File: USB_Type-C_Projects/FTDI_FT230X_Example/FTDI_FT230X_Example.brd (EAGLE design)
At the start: 32.5 x 65 mm, 47 parts, among them J1 105450-0101, U1 FT230XQ-R, U135123 P8X32A-Q44, U2 IRLML6401TRPBF, U3 NCP1117LPST33T3G, U4 CAT24C512WI-GT3, X1 ABMM-6.000MHZ-B2-T

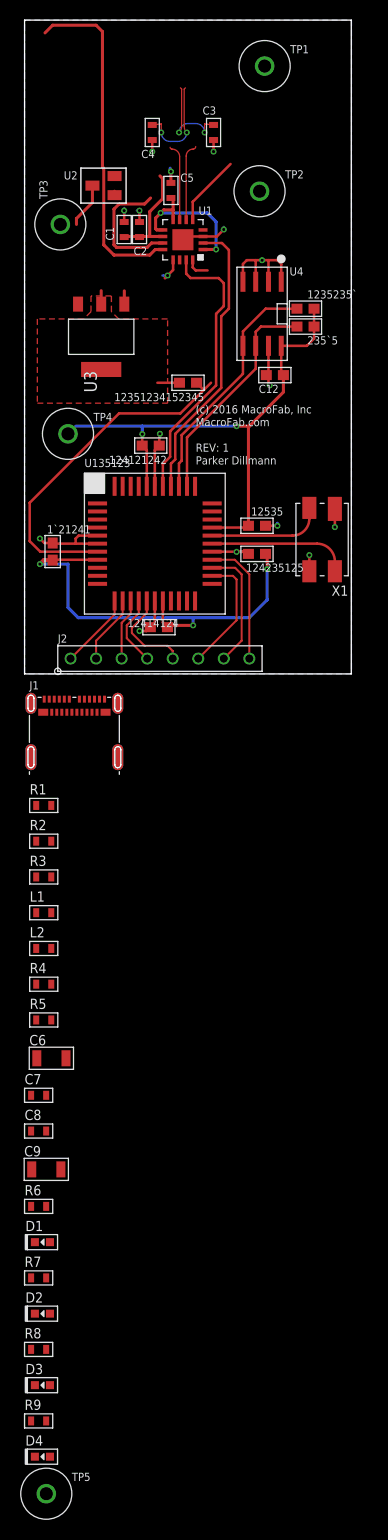
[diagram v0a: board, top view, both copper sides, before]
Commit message: Finished the FTDI_FT230X Example
Prop has been added and a header to monitor the current off the USB buss
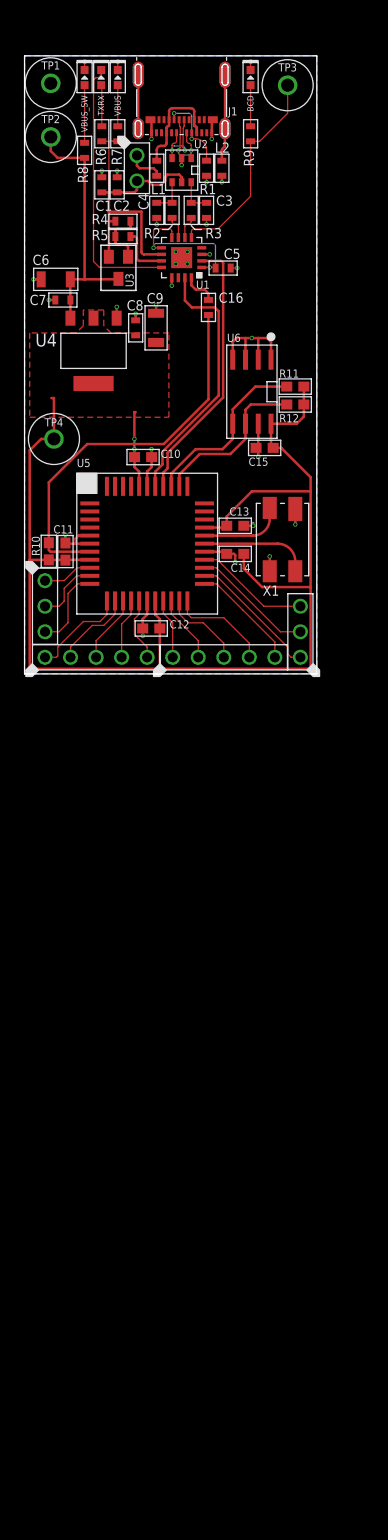
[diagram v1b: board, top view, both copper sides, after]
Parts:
- removed 12351234152345, 1235235`, 235`5: 10K, PP_Passives:0603
- removed 124121242, 12414124, 124235125, 12535, 1`21241: .1uF, PP_Passives:0603
- removed D1, D2, D3, D4: MF-LED-0603-RED, MF_LEDs:LED0603
- removed TP5: (no value), PP_Connectors:KEYSTONE_5115-5119
- removed U135123: P8X32A-Q44, PP_DigitalIC:P8X32A_LQFP-44
- added BCD, TXRX, VBUS, VBUS_SW: MF-LED-0603-RED, MF_LEDs:LED0603
- added C10, C11, C13, C14, C15: .1uF, PP_Passives:0603
- added C16: 0.1uF, MF_Passives:C0603
- added J3: MF-CON-2.54mm-01x02, MF_Connectors:PTH_2.54MM_01X02
- added J4, J6: MF-CON-2.54mm-01x05, MF_Connectors:PTH_2.54MM_01X05
- added J5: MF-CON-2.54mm-01x03, MF_Connectors:PTH_2.54MM_01X03
- added R10, R11, R12: 10K, PP_Passives:0603
- added U5: P8X32A-Q44, PP_DigitalIC:P8X32A_LQFP-44
- added U6: CAT24C512WI-GT3, PP_DigitalIC:SOIC-8_W
- FRAME1: value (none) -> MF_FRAMEDEFAULT
- J2: value (none) -> MF-CON-2.54mm-01x03; device PP_Connectors:2.54MM_01X08_PIN_HEADER -> MF_Connectors:PTH_2.54MM_01X03
- R6: value 150 -> 330
- TP1, TP2, TP3, TP4: value (none) -> 5115
- U2: value IRLML6401TRPBF -> IP4234CZ6,125; device PP_DiscreteSemi:SOT-23-3 -> PP_Passives:IP4234CZ6_SOT-457-6
- U3: value NCP1117LPST33T3G -> IRLML6401TRPBF; device MF_IC_Power:SOT-223-3 -> PP_DiscreteSemi:SOT-23-3
- U4: value CAT24C512WI-GT3 -> NCP1117LPST33T3G; device PP_DigitalIC:SOIC-8_W -> MF_IC_Power:SOT-223-3
- moved R9 129.7 mm to (22.5, 53.7), turned to 90 degrees
- moved R8 119.3 mm to (5.97, 52.1), turned to 90 degrees
- moved R7 114.1 mm to (9.27, 53.7), turned to 90 degrees
- moved R6 106.9 mm to (7.68, 53.7), turned to 90 degrees
- moved C9 84.4 mm to (13.1, 34.4), turned to 90 degrees
- moved C8 80.5 mm to (11.0, 34.4), turned to 90 degrees
- moved L2 79.6 mm to (19.6, 50.3), turned to 270 degrees
- moved C7 79.1 mm to (3.81, 37.2), turned to 180 degrees
- moved R5 78.3 mm to (9.78, 43.5)
- moved C6 77.5 mm to (3.10, 39.2), turned to 180 degrees
- moved R4 76.3 mm to (9.78, 45.0)
- moved L1 74.9 mm to (13.1, 50.3), turned to 270 degrees
- moved R3 67.9 mm to (16.6, 46.1), turned to 270 degrees
- moved R1 65.4 mm to (18.1, 50.3), turned to 270 degrees
- moved R2 64.0 mm to (14.7, 46.1), turned to 270 degrees
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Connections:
- net CC1/2 renamed CC1/1
- removed net N$1: D4.ANODE, R9.P$2
- removed net N$2: D1.ANODE, R6.P$2
- removed net N$41: R4.P$2, R5.P$1, U2.1
- removed net N$5: D2.ANODE, R7.P$2
- removed net N$6: D3.ANODE, R8.P$2
- new net N$10: R6.P$2, TXRX.ANODE
- new net N$11: R7.P$2, VBUS.ANODE
- new net N$12: R8.P$2, VBUS_SW.ANODE
- new net N$13: BCD.ANODE, R9.P$2
- new net N$14: C3.P$1, R3.P$1, U2.6
- new net N$15: C4.P$1, R2.P$1, U2.4
- new net N$8: R4.P$2, R5.P$1, U3.1
- new net SYSTEM_VBUS: C1.P$1, C2.P$1, J3.P$2, R4.P$1, R6.P$1, R7.P$1, U1.10, U2.5, U3.2
- net 3.3V: now also C10.2, C11.2, C13.2, C14.2, C15.2, R10.1, R11.2, R12.2, TP4.P$1, U4.P$1, U4.P$3, U5.18, U5.30, U5.40, U5.8, U6.8; no longer 12351234152345.2, 1235235`.2, 124121242.2, 12414124.2, 124235125.2, 12535.2, 1`21241.2, 235`5.2, R6.P$1, TP5.P$1, U135123.18, U135123.30, U135123.40, U135123.8, U3.P$1, U3.P$3, U4.8
- net BCD_CHARGER: now also TP3.P$1; no longer TP4.P$1
- net D+: now also U2.1; no longer C3.P$1, R3.P$1
- net D-: now also U2.3; no longer C4.P$1, R2.P$1
- net GND: now also BCD.CATHODE, C10.1, C11.1, C13.1, C14.1, C15.1, TP1.P$1, U2.2, U4.P$2, U5.17, U5.27, U5.39, U5.5, U5.6, U6.1, U6.2, U6.3, U6.4, U6.7, VBUS.CATHODE, VBUS_SW.CATHODE; no longer 124121242.1, 12414124.1, 124235125.1, 12535.1, 1`21241.1, D2.CATHODE, D3.CATHODE, D4.CATHODE, TP2.P$1, U135123.17, U135123.27, U135123.39, U135123.5, U135123.6, U3.P$2, U4.1, U4.2, U4.3, U4.4, U4.7
- net P0: now also U5.41; no longer U135123.41
- net P1: now also U5.42; no longer U135123.42
- net P10: now also J2.P$3, U5.11; no longer U135123.11
- net P11: now also J4.P$1, U5.12; no longer J2.1, U135123.12
- net P12: now also J4.P$2, U5.13; no longer J2.2, U135123.13
- net P13: now also J4.P$3, U5.14; no longer J2.3, U135123.14
- net P14: now also J4.P$4, U5.15; no longer J2.4, U135123.15
- net P15: now also J4.P$5, U5.16; no longer J2.5, U135123.16
- net P16: now also J6.P$1, U5.19; no longer U135123.19
- net P17: now also J6.P$2, U5.20; no longer U135123.20
- net P18: now also J6.P$3, U5.21; no longer U135123.21
- net P19: now also J6.P$4, U5.22; no longer U135123.22
- net P2: now also U5.43; no longer U135123.43
- net P20: now also J6.P$5, U5.23; no longer U135123.23
- net P21: now also J5.P$1, U5.24; no longer J2.6, U135123.24
- net P22: now also J5.P$2, U5.25; no longer J2.7, U135123.25
- net P23: now also J5.P$3, U5.26; no longer J2.8, U135123.26
- net P24: now also U5.31; no longer U135123.31
- net P25: now also U5.32; no longer U135123.32
- net P26: now also U5.33; no longer U135123.33
- net P27: now also U5.34; no longer U135123.34
- net P3: now also U5.44; no longer U135123.44
- net P4: now also U5.1; no longer U135123.1
- net P5: now also U5.2; no longer U135123.2
- net P6: now also U5.3; no longer U135123.3
- net P7: now also U5.4; no longer U135123.4
- net P8: now also J2.P$1, U5.9; no longer U135123.9
- net P9: now also J2.P$2, U5.10; no longer U135123.10
- net RES: now also C16.P$2, R10.2, U5.7; no longer 12351234152345.1, U135123.7
- net RTS: now also C16.P$1
- net RX: now also U5.37; no longer U135123.37
- net SCL: now also R12.1, U5.35, U6.6; no longer 235`5.1, U135123.35, U4.6
- net SDA: now also R11.1, U5.36, U6.5; no longer 1235235`.1, U135123.36, U4.5
- net TX: now also U5.38; no longer U135123.38
- net TX_RX_LED: now also TXRX.CATHODE; no longer D1.CATHODE
- net USB_VBUS: now also J3.P$1; no longer C1.P$1, C2.P$1, R4.P$1, R7.P$1, U1.10, U2.2
- net USB_VBUS_PORT: no longer TP1.P$1
- net USB_VBUS_SWITCHED: now also TP2.P$1, U3.3, U4.P$4; no longer TP3.P$1, U2.3, U3.P$4
- net X0: now also U5.29; no longer U135123.29
- net X1: now also U5.28; no longer U135123.28
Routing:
- net SYSTEM_VBUS: track 0.00 -> 34.3 mm
- net 3.3V: track 101.6 -> 132.4 mm, vias 5 -> 2
- net USB_VBUS_SWITCHED: track 4.73 -> 28.9 mm
- net N$9: track 0.00 -> 14.1 mm
- net BCD_CHARGER: track 7.09 -> 21.0 mm
- net P20: track 0.00 -> 10.9 mm
- net USB_VBUS_PORT: track 0.00 -> 10.6 mm
- net P19: track 0.00 -> 10.0 mm
- net CC1/1: track 0.00 -> 8.38 mm, vias 0 -> 2
- net P18: track 0.00 -> 8.33 mm
- net P10: track 0.00 -> 8.14 mm
- net PWREN: track 12.8 -> 5.21 mm
- net TX_RX_LED: track 34.1 -> 26.5 mm
- net USB_VBUS: track 10.7 -> 3.65 mm
- net P17: track 0.00 -> 6.71 mm
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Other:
- board size 32.5 x 65 mm -> 29.1 x 61.5 mm

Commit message: Added MPNs and normalized part values
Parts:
- C10, C11, C12, C13, C14, C15: value .1uF -> 0.1uF

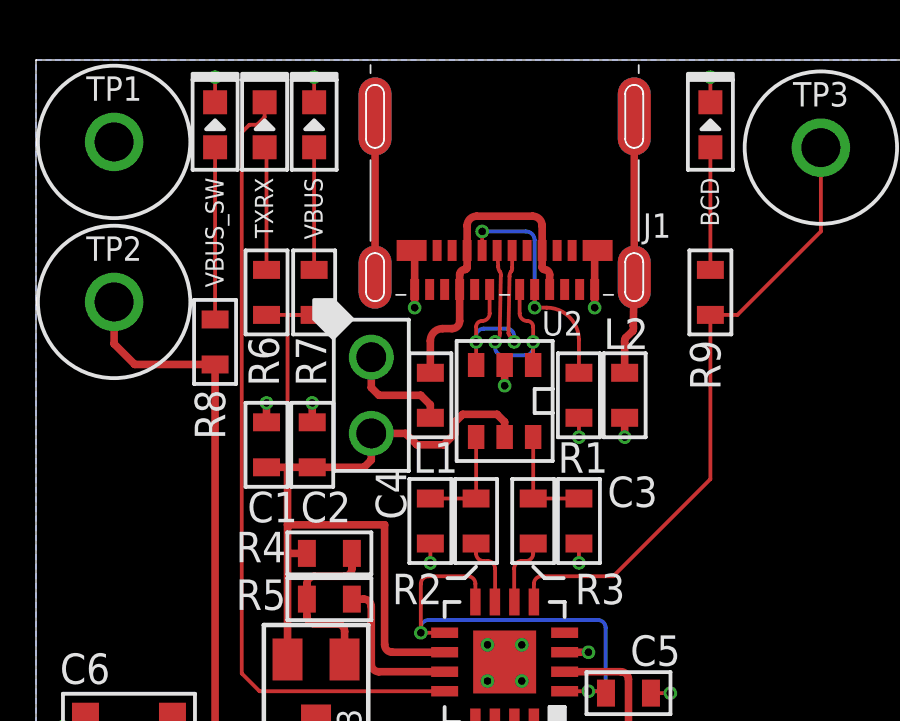
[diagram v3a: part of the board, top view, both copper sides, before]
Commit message: Fixed IP4234CZ6 ESD protection
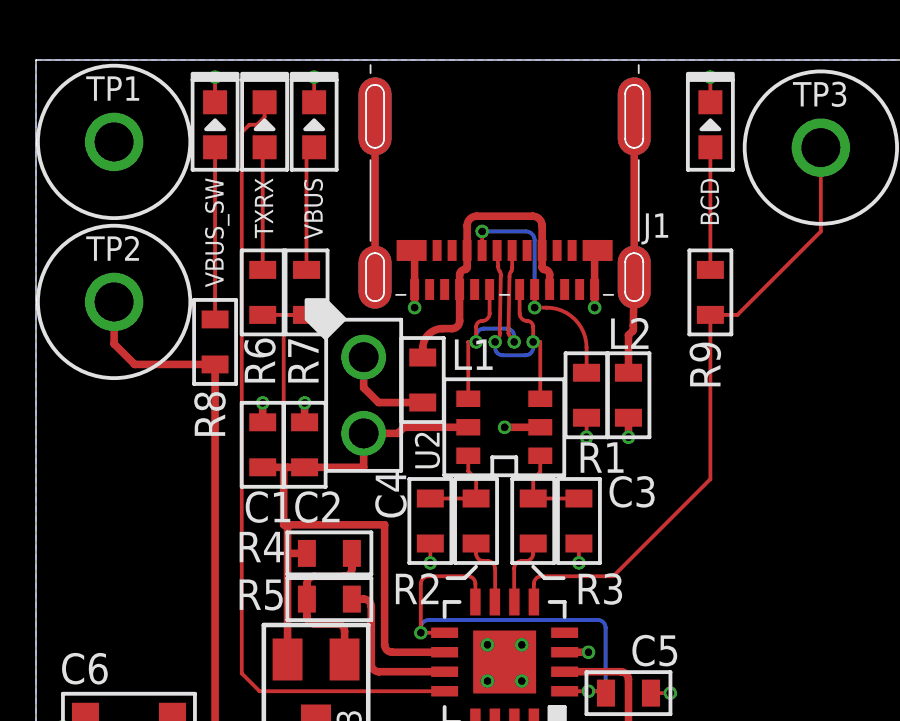
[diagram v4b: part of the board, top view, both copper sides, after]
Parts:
- moved U2 0.88 mm to (15.6, 49.2), turned to 180 degrees
- moved L1 0.57 mm to (12.9, 50.8)
- moved R1 0.25 mm to (18.4, 50.3)
- moved R7 0.25 mm to (9.02, 53.7)
- moved C2 0.25 mm to (8.95, 48.6)
- moved J3 0.25 mm to (10.9, 50.3)
- moved C1 0.13 mm to (7.56, 48.6)
- moved R6 0.13 mm to (7.56, 53.7)
- moved L2 0.13 mm to (19.7, 50.3)
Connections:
- net D+: now also U2.3; no longer U2.1
- net D-: now also U2.4; no longer U2.3
- net N$14: now also U2.1; no longer U2.6
- net N$15: now also U2.6; no longer U2.4
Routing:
- net SYSTEM_VBUS: track 34.3 -> 32.4 mm
- net D-: track 7.68 -> 9.07 mm
- net D+: track 7.68 -> 9.04 mm
- net N$14: track 3.58 -> 3.05 mm
- net N$15: track 3.58 -> 3.06 mm

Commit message: REV 2. Fixed USB ESD protection.
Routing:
- net SYSTEM_VBUS: track 32.4 -> 31.3 mm
- net 3.3V: track 132.4 -> 131.6 mm
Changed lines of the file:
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@@
 <?xml version="1.0" encoding="utf-8"?>
 <!DOCTYPE eagle SYSTEM "eagle.dtd">
-<eagle version="9.3.0">
+<eagle version="9.3.2">
 <drawing>
 <settings>
@@
 <attribute name="MPN" value="" x="0.889" y="11.176" size="1.778" layer="28" rot="MR180" display="off"/>
 <attribute name="POPULATE" value="0" x="0.889" y="11.176" size="1.778" layer="28" rot="MR180" display="off"/>
-<attribute name="REVNUM" value="REV: 1" x="0.889" y="16.256" size="0.8128" layer="22" font="vector" ratio="16" rot="MR180"/>
+<attribute name="REVNUM" value="REV: 2" x="0.889" y="16.256" size="0.8128" layer="22" font="vector" ratio="16" rot="MR180"/>
 <attribute name="URL" value="" x="0.889" y="11.176" size="1.778" layer="28" rot="MR180" display="off"/>
 </element>
@@
 <wire x1="1.651" y1="23.368" x2="0.508" y2="22.225" width="0.254" layer="1"/>
 <wire x1="0.508" y1="22.225" x2="0.508" y2="11.342" width="0.254" layer="1"/>
-<wire x1="0.508" y1="11.342" x2="0.508" y2="0.508" width="0.254" layer="1"/>
-<wire x1="0.508" y1="0.508" x2="13.4484" y2="0.508" width="0.254" layer="1"/>
-<wire x1="13.4484" y1="0.508" x2="28.448" y2="0.508" width="0.254" layer="1"/>
-<wire x1="28.448" y1="0.508" x2="28.448" y2="8.636" width="0.254" layer="1"/>
+<wire x1="0.508" y1="11.342" x2="0.508" y2="1.397" width="0.254" layer="1"/>
+<wire x1="0.508" y1="1.397" x2="1.397" y2="0.508" width="0.254" layer="1"/>
+<wire x1="1.397" y1="0.508" x2="13.4484" y2="0.508" width="0.254" layer="1"/>
+<wire x1="13.4484" y1="0.508" x2="27.94" y2="0.508" width="0.254" layer="1"/>
+<wire x1="27.94" y1="0.508" x2="28.448" y2="1.016" width="0.254" layer="1"/>
+<wire x1="28.448" y1="1.016" x2="28.448" y2="8.636" width="0.254" layer="1"/>
 <wire x1="28.448" y1="8.636" x2="28.448" y2="18.161" width="0.254" layer="1"/>
 <wire x1="28.448" y1="18.161" x2="28.448" y2="19.558" width="0.254" layer="1"/>
@@
 <contactref element="J1" pad="B6"/>
 <contactref element="U2" pad="3"/>
-<wire x1="16.571" y1="52.07" x2="16.8083" y2="52.07" width="0.127" layer="1"/>
-<wire x1="16.8083" y1="52.07" x2="16.8083" y2="50.1752" width="0.127" layer="1"/>
+<wire x1="16.571" y1="52.07" x2="16.8083" y2="51.8327" width="0.127" layer="1"/>
+<wire x1="16.8083" y1="51.8327" x2="16.8083" y2="50.1752" width="0.127" layer="1"/>
 </signal>
 <signal name="3V3OUT">
@@
 <contactref element="J1" pad="B7"/>
 <contactref element="U2" pad="4"/>
-<wire x1="14.671" y1="52.07" x2="14.4083" y2="52.07" width="0.127" layer="1"/>
-<wire x1="14.4083" y1="52.07" x2="14.4083" y2="50.1752" width="0.127" layer="1"/>
+<wire x1="14.671" y1="52.07" x2="14.4083" y2="51.8073" width="0.127" layer="1"/>
+<wire x1="14.4083" y1="51.8073" x2="14.4083" y2="50.1752" width="0.127" layer="1"/>
 </signal>
 <signal name="PWREN">
@@
 <wire x1="19.941" y1="59.589" x2="19.941" y2="54.10665" width="0.254" layer="1"/>
 <wire x1="19.941" y1="54.10665" x2="19.93678125" y2="54.10665" width="0.254" layer="1"/>
-<wire x1="11.301" y1="54.229" x2="19.7485" y2="52.297853125" width="0" layer="19" extent="1-1"/>
+<wire x1="11.301" y1="59.589" x2="19.941" y2="59.589" width="0" layer="19" extent="1-1"/>
 </signal>
 <signal name="BCD_CHARGER">
@@
 <wire x1="8.3845" y1="45.0215" x2="8.3845" y2="45.974" width="0.254" layer="1"/>
 <wire x1="9.029" y1="45.0215" x2="8.3845" y2="45.0215" width="0.254" layer="1"/>
-<wire x1="11.6205" y1="41.981" x2="11.6205" y2="45.974" width="0.254" layer="1"/>
-<wire x1="11.6205" y1="45.974" x2="8.3845" y2="45.974" width="0.254" layer="1"/>
+<wire x1="11.6205" y1="41.981" x2="11.6205" y2="45.4025" width="0.254" layer="1"/>
+<wire x1="11.6205" y1="45.4025" x2="11.049" y2="45.974" width="0.254" layer="1"/>
+<wire x1="11.049" y1="45.974" x2="8.3845" y2="45.974" width="0.254" layer="1"/>
 <contactref element="J3" pad="P$2"/>
 <contactref element="R6" pad="P$1"/>
@@
 <wire x1="7.5565" y1="52.971" x2="9.017" y2="52.971" width="0.127" layer="1"/>
 <wire x1="9.017" y1="52.971" x2="8.3845" y2="52.971" width="0.127" layer="1"/>
-<wire x1="10.922" y1="49.022" x2="10.922" y2="47.891" width="0.254" layer="1"/>
-<wire x1="10.922" y1="47.891" x2="8.9535" y2="47.891" width="0.254" layer="1"/>
+<wire x1="10.922" y1="49.022" x2="9.791" y2="47.891" width="0.254" layer="1"/>
+<wire x1="9.791" y1="47.891" x2="8.9535" y2="47.891" width="0.254" layer="1"/>
 <contactref element="U1" pad="10"/>
 <contactref element="C1" pad="P$1"/>
 <contactref element="C2" pad="P$1"/>
 <contactref element="U2" pad="5"/>
-<wire x1="8.3845" y1="45.974" x2="8.255" y2="45.974" width="0.254" layer="1"/>
-<wire x1="8.255" y1="45.974" x2="8.255" y2="47.891" width="0.254" layer="1"/>
+<wire x1="8.3845" y1="45.974" x2="8.255" y2="46.1035" width="0.254" layer="1"/>
+<wire x1="8.255" y1="46.1035" x2="8.255" y2="47.891" width="0.254" layer="1"/>
 <wire x1="9.017" y1="52.971" x2="8.255" y2="52.971" width="0.127" layer="1"/>
 <wire x1="8.255" y1="52.971" x2="8.255" y2="47.891" width="0.127" layer="1"/>
